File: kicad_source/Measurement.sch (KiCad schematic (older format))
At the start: 8 parts, among them CN5 691322310002, U4 LM75BD

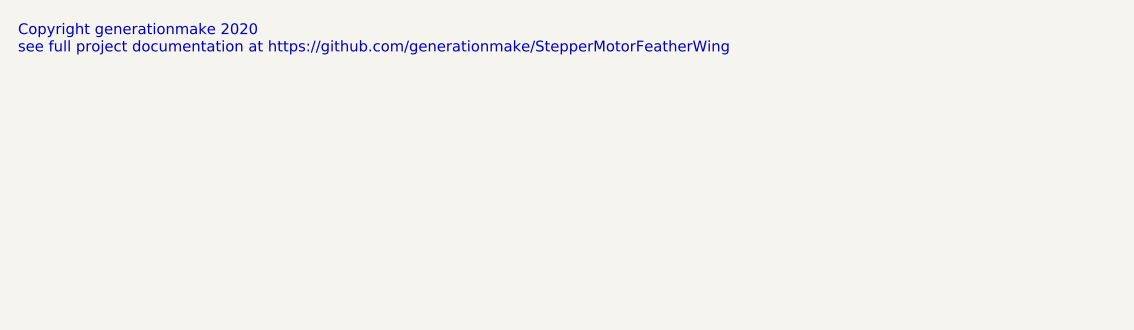
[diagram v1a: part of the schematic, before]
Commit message: corrected links and titles, generated schematic pdf and net list
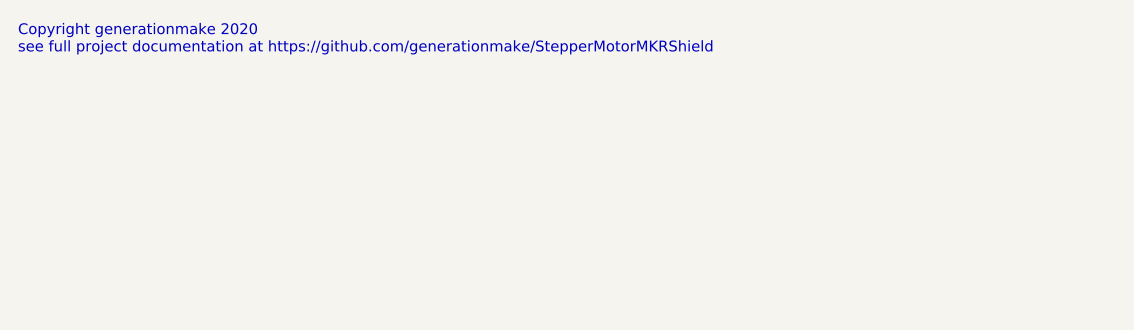
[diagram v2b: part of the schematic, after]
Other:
- note added: "Copyright generationmake 2020\nsee full project documentation at https://github.com/generationmake/StepperMotorMKRShield"
- note removed: "Copyright generationmake 2020\nsee full project documentation at https://github.com/generationmake/StepperMotorFeatherWing"
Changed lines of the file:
@@
 encoding utf-8
 Sheet 2 6
-Title "StepperMotorFeatherWing"
-Date "2020-07-11"
+Title "StepperMotorMKRShield"
+Date "2020-07-12"
 Rev "1.1"
 Comp "generationmake"
@@
 $EndDescr
 Text Notes 500  650  0    47   ~ 0
-Copyright generationmake 2020\nsee full project documentation at https://github.com/generationmake/StepperMotorFeatherWing
+Copyright generationmake 2020\nsee full project documentation at https://github.com/generationmake/StepperMotorMKRShield
 Text Notes 7000 6900 0    43   ~ 0
 You may redistribute and modify this documentation under the terms of the CERN OHL v.1.2. (http://ohwr.org/cernohl). \nThis documentation is distributed WITHOUT ANY EXPRESS OR IMPLIED WARRANTY, INCLUDING OF MERCHANTABILITY, SATISFACTORY \nQUALITY AND FITNESS FOR A PARTICULAR PURPOSE. Please see the CERN OHL v.1.2  for applicable conditions
